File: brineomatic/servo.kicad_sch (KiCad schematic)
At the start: 8 parts, among them J8 SERVOS, U2 XL1509-5.0

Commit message: worked on schematic and layout a bit more.
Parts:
- C4: footprint Capacitor_SMD:C_0805_2012Metric_Pad1.18x1.45mm_HandSolder -> Capacitor_SMD:C_0603_1608Metric
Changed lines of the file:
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@@
 			)
 		)
-		(property "Footprint" "Capacitor_SMD:C_0805_2012Metric_Pad1.18x1.45mm_HandSolder"
+		(property "Footprint" "Capacitor_SMD:C_0603_1608Metric"
 			(at 67.31 134.62 0)
 			(effects

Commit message: lots of progress on Rev B
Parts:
- removed C4: 100nF, Capacitor_SMD:C_0603_1608Metric, symbol Device:C_Small
- removed C5: 10uF/35v, Capacitor_SMD:C_1206_3216Metric_Pad1.33x1.80mm_HandSolder, symbol Device:C_Small
- removed C6: 100uF / 10v, Capacitor_Tantalum_SMD:CP_EIA-3528-21_Kemet-B, symbol Device:C_Polarized_Small_US
- removed D3: DSK34, Diode_SMD:D_SOD-123, symbol Device:D_Schottky
- removed F1: mSMD150, Fuse:Fuse_1812_4532Metric_Pad1.30x3.40mm_HandSolder, symbol Device:Polyfuse_Small
- removed L1: 2.5A 68uH, Inductor_SMD:L_Sunlord_MWSA1003S, symbol Device:L
- removed U2: XL1509-5.0, Package_SO:SOIC-8_3.9x4.9mm_P1.27mm, symbol Regulator_Switching:XL1509-5.0
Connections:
- net +5V: now reaches J8.3 (Pin_3), J8.4 (Pin_4)

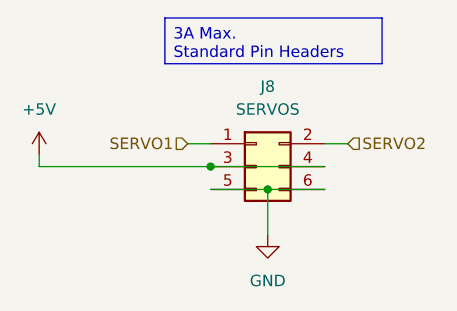
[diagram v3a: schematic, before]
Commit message: tmc2209 driver schematic checked and laid out nicely.
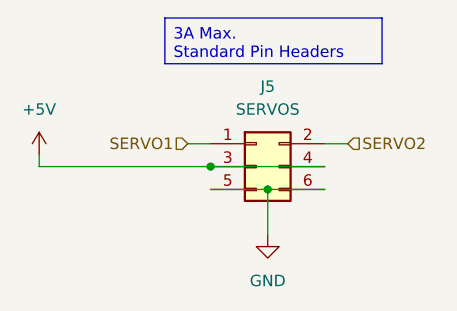
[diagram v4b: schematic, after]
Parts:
- renumbered J8 to J5
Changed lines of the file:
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@@
 		(dnp no)
 		(fields_autoplaced yes)
-		(property "Reference" "#PWR09"
+		(property "Reference" "#PWR017"
 			(at 149.86 129.54 0)
 			(effects
@@
 			(project ""
 				(path "/96477ae2-ef08-48f3-8dd4-fe4478541f68/0442c100-f200-44e3-9806-ad19ad5a87d8"
-					(reference "#PWR09")
+					(reference "#PWR017")
 					(unit 1)
 				)
@@
 		(dnp no)
 		(fields_autoplaced yes)
-		(property "Reference" "J8"
+		(property "Reference" "J5"
 			(at 175.26 118.11 0)
 			(effects
@@
 			(project ""
 				(path "/96477ae2-ef08-48f3-8dd4-fe4478541f68/0442c100-f200-44e3-9806-ad19ad5a87d8"
-					(reference "J8")
+					(reference "J5")
 					(unit 1)
 				)
@@
 		(dnp no)
 		(fields_autoplaced yes)
-		(property "Reference" "#PWR017"
+		(property "Reference" "#PWR018"
 			(at 175.26 140.97 0)
 			(effects
@@
 			(project "brineomatic"
 				(path "/96477ae2-ef08-48f3-8dd4-fe4478541f68/0442c100-f200-44e3-9806-ad19ad5a87d8"
-					(reference "#PWR017")
+					(reference "#PWR018")
 					(unit 1)
 				)

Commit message: worked on bom for rev b prototype run
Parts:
- J5: value SERVOS -> ~
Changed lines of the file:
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@@
 			)
 		)
-		(property "Value" "SERVOS"
+		(property "Value" "~"
 			(at 175.26 120.65 0)
 			(effects

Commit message: updated jlc parts rotations and placement offsets
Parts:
- J5: Rotation Offset (none) -> 270
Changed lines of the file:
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@@
+			)
+		)
+		(property "Rotation Offset" "270"
+			(at 173.99 127 0)
+			(effects
+				(font
+					(size 1.27 1.27)
+				)
+				(hide yes)
 			)
 		)

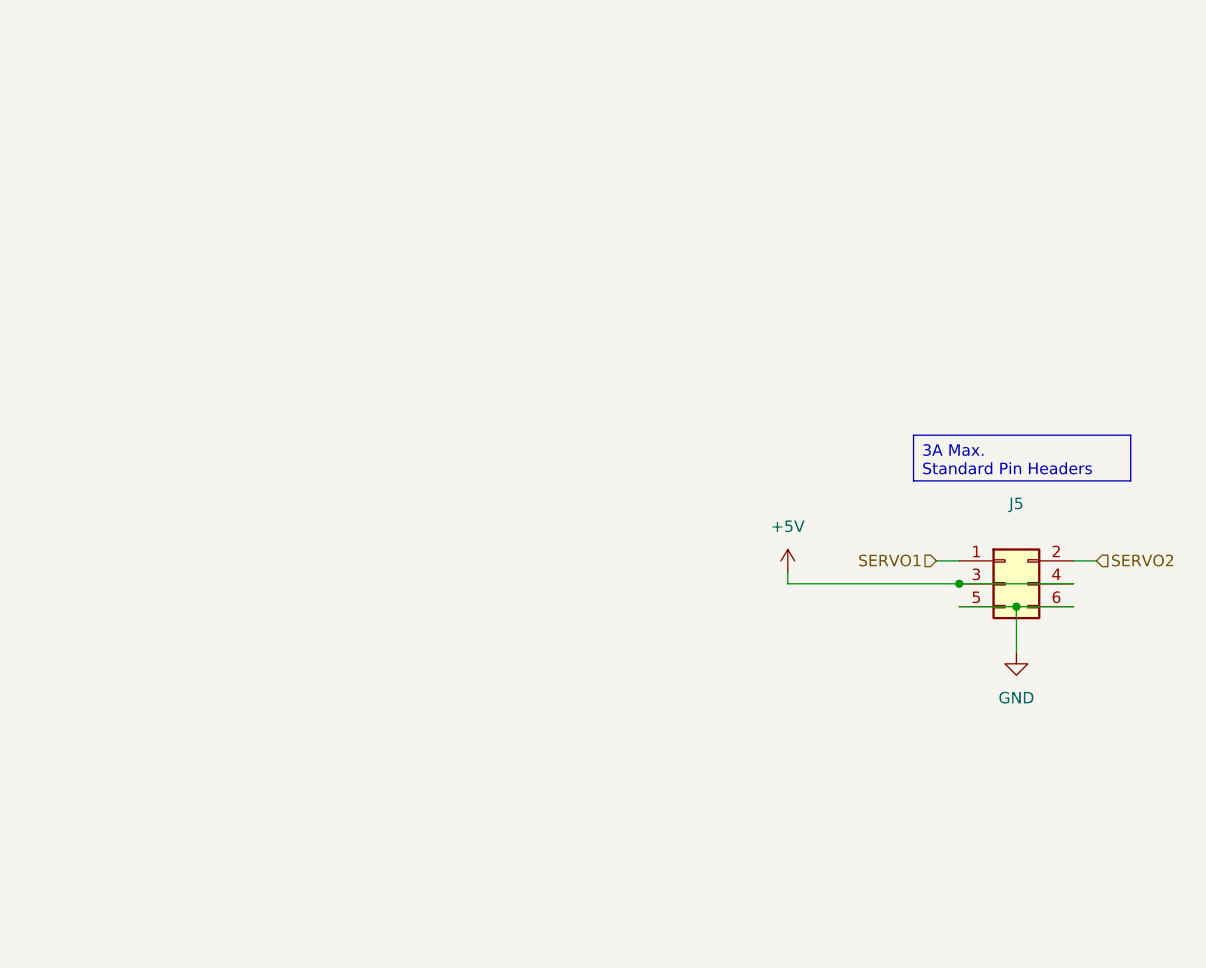
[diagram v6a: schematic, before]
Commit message: added qwiic i2c connector
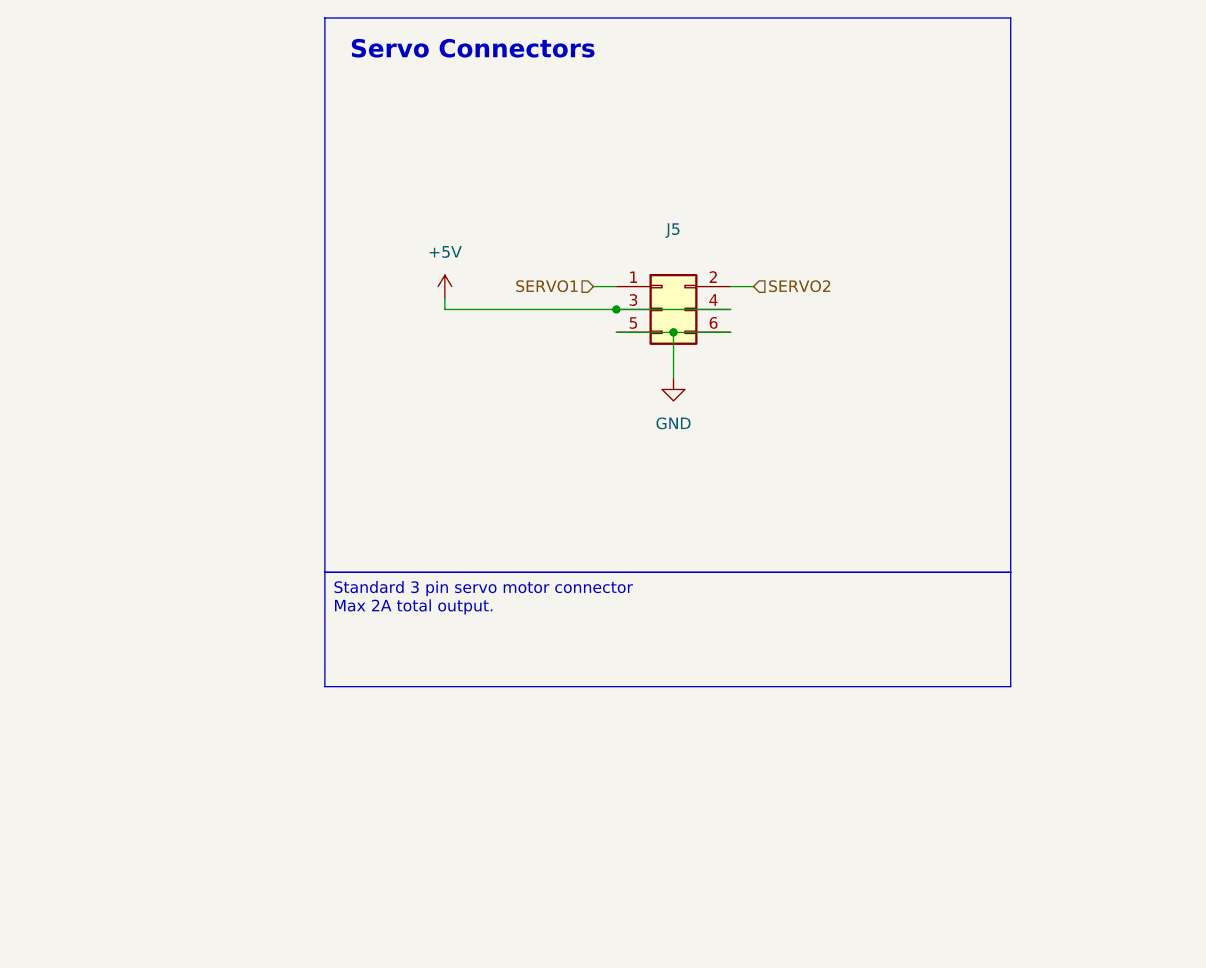
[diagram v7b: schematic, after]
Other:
- note added: "Servo Connectors"
- title: (none) -> https://github.com/hoeken/brineomatic
- moved on the sheet: J5
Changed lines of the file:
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@@
 	(generator_version "9.0")
 	(paper "A4")
-	(text_box "3A Max.\nStandard Pin Headers"
-		(exclude_from_sim no)
-		(at 163.83 110.49 0)
-		(size 24.13 5.08)
+	(title_block
+		(title "https://github.com/hoeken/brineomatic")
+		(date "2025-08-28")
+		(rev "B")
+	)
+	(rectangle
+		(start 98.425 64.135)
+		(end 174.625 125.73)
+		(stroke
+			(width 0)
+			(type default)
+		)
+		(fill
+			(type none)
+		)
+	)
+	(text "Servo Connectors"
+		(exclude_from_sim no)
+		(at 101.219 67.818 0)
+		(effects
+			(font
+				(size 2 2)
+				(thickness 0.4)
+				(bold yes)
+			)
+			(justify left)
+		)
+	)
+	(text_box "Standard 3 pin servo motor connector\nMax 2A total output."
+		(exclude_from_sim no)
+		(at 98.425 125.73 0)
+		(size 76.2 12.7)
 		(margins 0.9525 0.9525 0.9525 0.9525)
 		(stroke
 			(width 0)
-			(type default)
+			(type solid)
 		)
 		(fill
@@
 	)
 	(junction
-		(at 175.26 129.54)
+		(at 137.16 99.06)
 		(diameter 0)
 		(color 0 0 0 0)
 	)
 	(junction
-		(at 168.91 127)
+		(at 130.81 96.52)
 		(diameter 0)
 		(color 0 0 0 0)
@@
 	(wire
 		(pts
-			(xy 168.91 127) (xy 149.86 127)
-		)
-		(stroke
-			(width 0)
-			(type default)
-		)
-	)
-	(wire
-		(pts
-			(xy 175.26 129.54) (xy 175.26 134.62)
-		)
-		(stroke
-			(width 0)
-			(type default)
-		)
-	)
-	(wire
-		(pts
-			(xy 168.91 124.46) (xy 166.37 124.46)
-		)
-		(stroke
-			(width 0)
-			(type default)
-		)
-	)
-	(wire
-		(pts
-			(xy 175.26 129.54) (xy 181.61 129.54)
-		)
-		(stroke
-			(width 0)
-			(type default)
-		)
-	)
-	(wire
-		(pts
-			(xy 168.91 127) (xy 181.61 127)
-		)
-		(stroke
-			(width 0)
-			(type default)
-		)
-	)
-	(wire
-		(pts
-			(xy 175.26 129.54) (xy 168.91 129.54)
-		)
-		(stroke
-			(width 0)
-			(type default)
-		)
-	)
-	(wire
-		(pts
-			(xy 181.61 124.46) (xy 184.15 124.46)
-		)
-		(stroke
-			(width 0)
-			(type default)
-		)
-	)
-	(wire
-		(pts
-			(xy 149.86 127) (xy 149.86 125.73)
+			(xy 130.81 96.52) (xy 111.76 96.52)
+		)
+		(stroke
+			(width 0)
+			(type default)
+		)
+	)
+	(wire
+		(pts
+			(xy 137.16 99.06) (xy 137.16 104.14)
+		)
+		(stroke
+			(width 0)
+			(type default)
+		)
+	)
+	(wire
+		(pts
+			(xy 130.81 93.98) (xy 128.27 93.98)
+		)
+		(stroke
+			(width 0)
+			(type default)
+		)
+	)
+	(wire
+		(pts
+			(xy 137.16 99.06) (xy 143.51 99.06)
+		)
+		(stroke
+			(width 0)
+			(type default)
+		)
+	)
+	(wire
+		(pts
+			(xy 130.81 96.52) (xy 143.51 96.52)
+		)
+		(stroke
+			(width 0)
+			(type default)
+		)
+	)
+	(wire
+		(pts
+			(xy 137.16 99.06) (xy 130.81 99.06)
+		)
+		(stroke
+			(width 0)
+			(type default)
+		)
+	)
+	(wire
+		(pts
+			(xy 143.51 93.98) (xy 146.05 93.98)
+		)
+		(stroke
+			(width 0)
+			(type default)
+		)
+	)
+	(wire
+		(pts
+			(xy 111.76 96.52) (xy 111.76 95.25)
 		)
 		(stroke
@@
 	(hierarchical_label "SERVO1"
 		(shape input)
-		(at 166.37 124.46 180)
+		(at 128.27 93.98 180)
 		(effects
 			(font
@@
 	(hierarchical_label "SERVO2"
 		(shape input)
-		(at 184.15 124.46 0)
+		(at 146.05 93.98 0)
 		(effects
 			(font
@@
 	(symbol
 		(lib_id "power:+5V")
-		(at 149.86 125.73 0)
+		(at 111.76 95.25 0)
 		(unit 1)
 		(exclude_from_sim no)
@@
 		(fields_autoplaced yes)
 		(property "Reference" "#PWR017"
-			(at 149.86 129.54 0)
+			(at 111.76 99.06 0)
 			(effects
 				(font
@@
 		)
 		(property "Value" "+5V"
-			(at 149.86 120.65 0)
+			(at 111.76 90.17 0)
 			(effects
 				(font
@@
 		)
 		(property "Footprint" ""
-			(at 149.86 125.73 0)
+			(at 111.76 95.25 0)
 			(effects
 				(font
@@
 		)
 		(property "Datasheet" ""
-			(at 149.86 125.73 0)
+			(at 111.76 95.25 0)
 			(effects
 				(font
@@
 		)
 		(property "Description" "Power symbol creates a global label with name \"+5V\""
-			(at 149.86 125.73 0)
+			(at 111.76 95.25 0)
 			(effects
 				(font
@@
 	(symbol
 		(lib_id "Connector_Generic:Conn_02x03_Odd_Even")
-		(at 173.99 127 0)
+		(at 135.89 96.52 0)
 		(unit 1)
 		(exclude_from_sim no)
@@
 		(fields_autoplaced yes)
 		(property "Reference" "J5"
-			(at 175.26 118.11 0)
+			(at 137.16 87.63 0)
 			(effects
 				(font
@@
 		)
 		(property "Value" "~"
-			(at 175.26 120.65 0)
+			(at 137.16 90.17 0)
 			(effects
 				(font
@@
 		)
 		(property "Footprint" "Connector_PinHeader_2.54mm:PinHeader_2x03_P2.54mm_Horizontal"
-			(at 173.99 127 0)
+			(at 135.89 96.52 0)
 			(effects
 				(font
@@
 		)
 		(property "Datasheet" "~"
-			(at 173.99 127 0)
+			(at 135.89 96.52 0)
 			(effects
 				(font
@@
 		)
 		(property "Description" "Generic connector, double row, 02x03, odd/even pin numbering scheme (row 1 odd numbers, row 2 even numbers), script generated (kicad-library-utils/schlib/autogen/connector/)"
-			(at 173.99 127 0)
+			(at 135.89 96.52 0)
 			(effects
 				(font
@@
 		)
 		(property "LCSC" "C239334"
-			(at 173.99 127 0)
+			(at 135.89 96.52 0)
 			(effects
 				(font
@@
 		)
 		(property "Rotation Offset" "270"
-			(at 173.99 127 0)
+			(at 135.89 96.52 0)
 			(effects
 				(font
@@
 	(symbol
 		(lib_id "power:GND")
-		(at 175.26 134.62 0)
+		(at 137.16 104.14 0)
 		(mirror y)
 		(unit 1)
@@
 		(fields_autoplaced yes)
 		(property "Reference" "#PWR018"
-			(at 175.26 140.97 0)
+			(at 137.16 110.49 0)
 			(effects
 				(font
@@
 		)
 		(property "Value" "GND"
-			(at 175.26 139.7 0)
+			(at 137.16 109.22 0)
 			(effects
 				(font
@@
 		)
 		(property "Footprint" ""
-			(at 175.26 134.62 0)
+			(at 137.16 104.14 0)
 			(effects
 				(font
@@
 		)
 		(property "Datasheet" ""
-			(at 175.26 134.62 0)
+			(at 137.16 104.14 0)
 			(effects
 				(font
@@
 		)
 		(property "Description" "Power symbol creates a global label with name \"GND\" , ground"
-			(at 175.26 134.62 0)
-			(effects
-				(font
+			(at 137.16 104.14 0)
+			(effects
+				(font

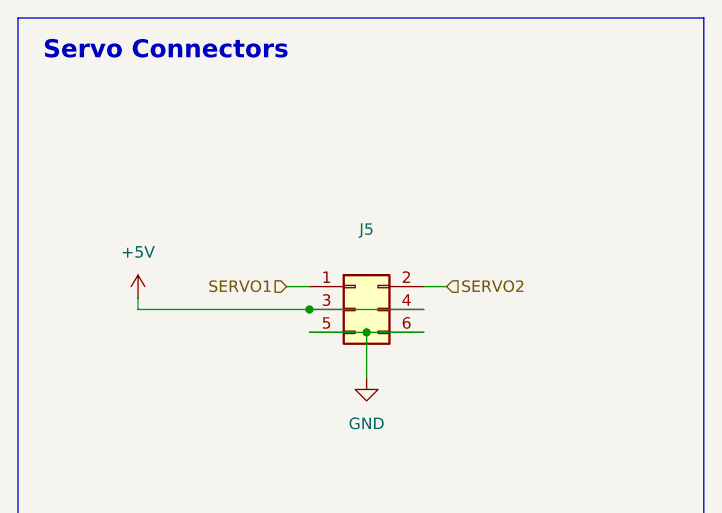
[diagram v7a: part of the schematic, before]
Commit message: added pullup resistor to adc alert
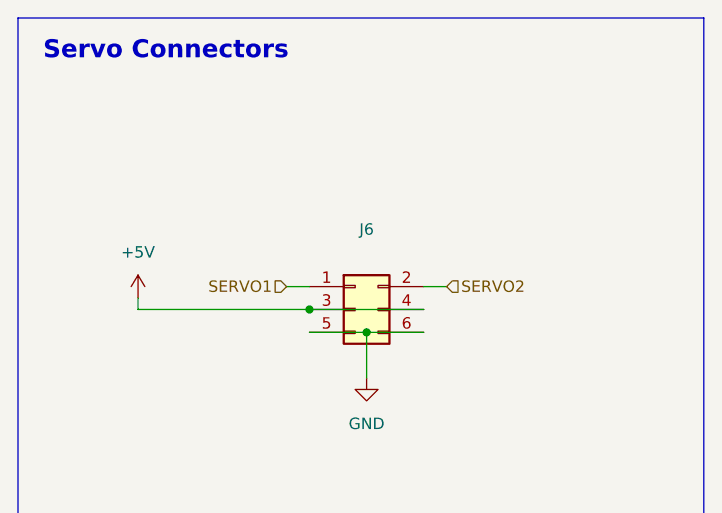
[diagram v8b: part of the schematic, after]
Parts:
- renumbered J5 to J6
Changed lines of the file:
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@@
 		(dnp no)
 		(fields_autoplaced yes)
-		(property "Reference" "#PWR017"
+		(property "Reference" "#PWR019"
 			(at 111.76 99.06 0)
 			(effects
@@
 			(project ""
 				(path "/96477ae2-ef08-48f3-8dd4-fe4478541f68/0442c100-f200-44e3-9806-ad19ad5a87d8"
-					(reference "#PWR017")
+					(reference "#PWR019")
 					(unit 1)
 				)
@@
 		(dnp no)
 		(fields_autoplaced yes)
-		(property "Reference" "J5"
+		(property "Reference" "J6"
 			(at 137.16 87.63 0)
 			(effects
@@
 			(project ""
 				(path "/96477ae2-ef08-48f3-8dd4-fe4478541f68/0442c100-f200-44e3-9806-ad19ad5a87d8"
-					(reference "J5")
+					(reference "J6")
 					(unit 1)
 				)
@@
 		(dnp no)
 		(fields_autoplaced yes)
-		(property "Reference" "#PWR018"
+		(property "Reference" "#PWR020"
 			(at 137.16 110.49 0)
 			(effects
@@
 			(project "brineomatic"
 				(path "/96477ae2-ef08-48f3-8dd4-fe4478541f68/0442c100-f200-44e3-9806-ad19ad5a87d8"
-					(reference "#PWR018")
+					(reference "#PWR020")
 					(unit 1)
 				)
